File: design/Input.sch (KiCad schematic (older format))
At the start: 36 parts, among them J501 Conn_01x03, U501 93C46B, U502 FT4232H, U503 74LV595, X501 ASEMB-12MHz

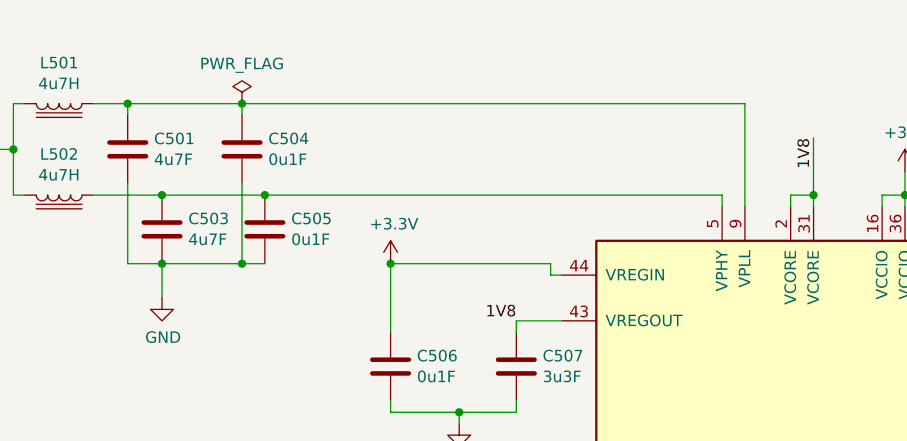
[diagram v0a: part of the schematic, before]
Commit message: Add 5V power to USB isolator
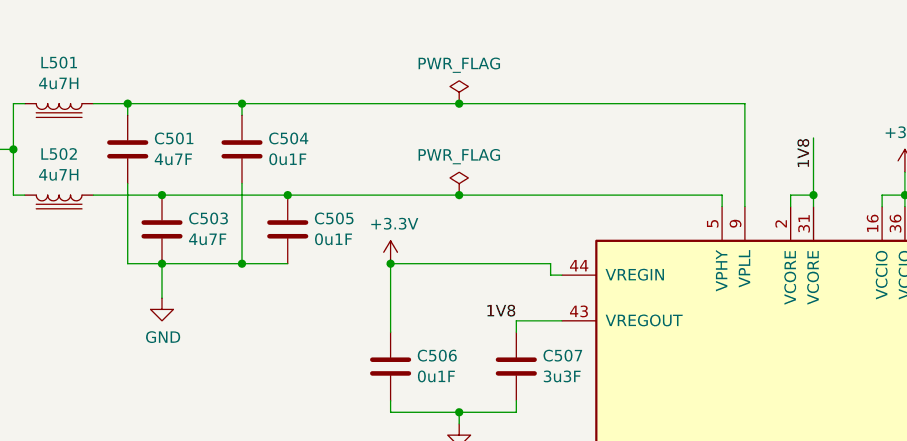
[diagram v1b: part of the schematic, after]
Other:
- moved on the sheet: C505
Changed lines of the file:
@@
 L Device:C C505
 U 1 1 5A772A13
-P 2500 1550
+P 2600 1550
 AR Path="/5A78E64E/5A772A13" Ref="C505"  Part="1"
 AR Path="/5A78E661/5A772A13" Ref="C705"  Part="1"
-F 0 "C505" H 2615 1596 50  0000 L CNN
-F 1 "0u1F" H 2615 1505 50  0000 L CNN
-F 2 "Capacitor_SMD:C_0603_1608Metric" H 2538 1400 50  0001 C CNN
-F 3 "http://www.samsungsem.com/kr/support/product-search/mlcc/CL10B104KO8WPNC.jsp" H 2500 1550 50  0001 C CNN
-F 4 "CL10B104KO8WPNC" H 2500 1550 50  0001 C CNN "mpn"
-	1    2500 1550
+F 0 "C505" H 2715 1596 50  0000 L CNN
+F 1 "0u1F" H 2715 1505 50  0000 L CNN
+F 2 "Capacitor_SMD:C_0603_1608Metric" H 2638 1400 50  0001 C CNN
+F 3 "http://www.samsungsem.com/kr/support/product-search/mlcc/CL10B104KO8WPNC.jsp" H 2600 1550 50  0001 C CNN
+F 4 "CL10B104KO8WPNC" H 2600 1550 50  0001 C CNN "mpn"
+	1    2600 1550
 	1    0    0    -1
 $EndComp
@@
 L power:PWR_FLAG #FLG0501
 U 1 1 5A8B20A8
-P 2400 1000
+P 3350 1000
 AR Path="/5A78E64E/5A8B20A8" Ref="#FLG0501"  Part="1"
 AR Path="/5A78E661/5A8B20A8" Ref="#FLG0701"  Part="1"
-F 0 "#FLG0701" H 2400 1075 50  0001 C CNN
-F 1 "PWR_FLAG" H 2400 1174 50  0000 C CNN
-F 2 "" H 2400 1000 50  0001 C CNN
-F 3 "" H 2400 1000 50  0001 C CNN
-	1    2400 1000
+F 0 "#FLG0701" H 3350 1075 50  0001 C CNN
+F 1 "PWR_FLAG" H 3350 1174 50  0000 C CNN
+F 2 "" H 3350 1000 50  0001 C CNN
+F 3 "" H 3350 1000 50  0001 C CNN
+	1    3350 1000
 	1    0    0    -1
 $EndComp
@@
 	1750 1400 2050 1400
 Wire Wire Line
-	2400 1000 4600 1000
-Wire Wire Line
-	2500 1400 4500 1400
-Wire Wire Line
-	2050 1400 2500 1400
+	2400 1000 3350 1000
+Wire Wire Line
+	2600 1400 3350 1400
 Connection ~ 2050 1400
 Connection ~ 1900 1000
@@
 Wire Wire Line
 	2050 1700 1900 1700
-Connection ~ 2500 1400
-Wire Wire Line
-	2400 1700 2500 1700
+Wire Wire Line
+	2400 1700 2600 1700
 Connection ~ 2400 1700
 Wire Wire Line
@@
 NoConn ~ 9550 3300
 NoConn ~ 9350 3300
+Connection ~ 2600 1400
+Wire Wire Line
+	2050 1400 2600 1400
+$Comp
+L power:PWR_FLAG #FLG0103
+U 1 1 5A985F6D
+P 3350 1400
+AR Path="/5A78E64E/5A985F6D" Ref="#FLG0103"  Part="1"
+AR Path="/5A78E661/5A985F6D" Ref="#FLG0104"  Part="1"
+F 0 "#FLG0104" H 3350 1475 50  0001 C CNN
+F 1 "PWR_FLAG" H 3350 1574 50  0000 C CNN
+F 2 "" H 3350 1400 50  0001 C CNN
+F 3 "" H 3350 1400 50  0001 C CNN
+	1    3350 1400
+	1    0    0    -1
+$EndComp
+Connection ~ 3350 1400
+Wire Wire Line
+	3350 1400 4500 1400
+Connection ~ 3350 1000
+Wire Wire Line
+	3350 1000 4600 1000
 $EndSCHEMATC

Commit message: Minimizing space in design
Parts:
- D501, D502, D503: footprint LED_THT:LED_D5.0mm-3 -> LEDs:WP130WDT
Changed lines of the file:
@@
 F 0 "D701" H 10550 3500 50  0000 C CNN
 F 1 "WP130WDT/EGW" H 10550 3584 50  0001 C CNN
-F 2 "LED_THT:LED_D5.0mm-3" H 10550 3250 50  0001 C CNN
+F 2 "LEDs:WP130WDT" H 10550 3250 50  0001 C CNN
 F 3 "http://www.kingbrightusa.com/images/catalog/SPEC/WP130WDT-EGW.pdf" H 10550 3250 50  0001 C CNN
 F 4 "WP130WDT/EGW" H 10550 3250 50  0001 C CNN "mpn"
@@
 F 0 "D702" H 10550 4000 50  0000 C CNN
 F 1 "WP130WDT/EGW" H 10550 4084 50  0001 C CNN
-F 2 "LED_THT:LED_D5.0mm-3" H 10550 3750 50  0001 C CNN
+F 2 "LEDs:WP130WDT" H 10550 3750 50  0001 C CNN
 F 3 "http://www.kingbrightusa.com/images/catalog/SPEC/WP130WDT-EGW.pdf" H 10550 3750 50  0001 C CNN
 F 4 "WP130WDT/EGW" H 10550 3750 50  0001 C CNN "mpn"
@@
 F 0 "D703" H 10550 4500 50  0000 C CNN
 F 1 "WP130WDT/EGW" H 10550 4584 50  0001 C CNN
-F 2 "LED_THT:LED_D5.0mm-3" H 10550 4250 50  0001 C CNN
+F 2 "LEDs:WP130WDT" H 10550 4250 50  0001 C CNN
 F 3 "http://www.kingbrightusa.com/images/catalog/SPEC/WP130WDT-EGW.pdf" H 10550 4250 50  0001 C CNN
 F 4 "WP130WDT/EGW" H 10550 4250 50  0001 C CNN "mpn"

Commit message: Switching to light pipes for LEDs
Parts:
- removed D502, D503: WP130WDT/EGW, LEDs:WP130WDT, symbol Device:LED_Dual_ACA
- added D502, D503: LTST-C155GYKT, LED_SMD:LED_RGB_1210, symbol Device:LED_Dual_AACC
- added LP501: LightPipe, LEDs:LightPipe DiaLight 515-1064, symbol CommsCard:LightPipe
- D501: value WP130WDT/EGW -> LTST-C155GYKT; footprint LEDs:WP130WDT -> LED_SMD:LED_RGB_1210; symbol Device:LED_Dual_ACA -> Device:LED_Dual_AACC; mpn WP130WDT/EGW -> LTST-C155GYKT
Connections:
- net GND: now also D503.3 (K1); no longer D501.2 (K)
- net at RN501.11 (R6.2): now also D501.2 (A2); no longer D501.1 (A1)
- net at RN501.12 (R5.2): now also D501.1 (A1); no longer D501.3 (A2)
- net at RN501.13 (R4.2): now also D502.2 (A2)
- net at RN501.14 (R3.2): now also D502.1 (A1)
- net at RN501.15 (R2.2): now also D503.2 (A2)
- net at RN501.16 (R1.2): now also D503.1 (A1)
- new net: D501.3 (K1), D501.4 (K2), D502.4 (K2)
- new net: D502.3 (K1), D503.4 (K2)
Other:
- moved on the sheet: D701
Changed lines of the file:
@@
 $Descr A4 11693 8268
 encoding utf-8
-Sheet 7 10
+Sheet 5 10
 Title ""
 Date ""
@@
 NoConn ~ 9950 3400
 $Comp
-L Device:LED_Dual_ACA D501
+L Device:LED_Dual_AACC D501
 U 1 1 5A834768
 P 10550 3250
@@
 AR Path="/5A78E661/5A834768" Ref="D701"  Part="1"
 F 0 "D701" H 10550 3500 50  0000 C CNN
-F 1 "WP130WDT/EGW" H 10550 3584 50  0001 C CNN
-F 2 "LEDs:WP130WDT" H 10550 3250 50  0001 C CNN
-F 3 "http://www.kingbrightusa.com/images/catalog/SPEC/WP130WDT-EGW.pdf" H 10550 3250 50  0001 C CNN
-F 4 "WP130WDT/EGW" H 10550 3250 50  0001 C CNN "mpn"
+F 1 "LTST-C155GYKT" H 10550 3584 50  0001 C CNN
+F 2 "LED_SMD:LED_RGB_1210" H 10550 3250 50  0001 C CNN
+F 3 "http://optoelectronics.liteon.com/upload/download/DS-22-98-0007/LTST-C155GYKT.pdf" H 10550 3250 50  0001 C CNN
+F 4 "LTST-C155GYKT" H 10550 3250 50  0001 C CNN "mpn"
 	1    10550 3250
-	-1   0    0    -1
+	1    0    0    1
 $EndComp
 $Comp
@@
 	1    0    0    -1
 $EndComp
-Wire Wire Line
-	10850 3250 10850 3750
-$Comp
-L Device:LED_Dual_ACA D502
-U 1 1 5A83C5E4
-P 10550 3750
-AR Path="/5A78E64E/5A83C5E4" Ref="D502"  Part="1"
-AR Path="/5A78E661/5A83C5E4" Ref="D702"  Part="1"
-F 0 "D702" H 10550 4000 50  0000 C CNN
-F 1 "WP130WDT/EGW" H 10550 4084 50  0001 C CNN
-F 2 "LEDs:WP130WDT" H 10550 3750 50  0001 C CNN
-F 3 "http://www.kingbrightusa.com/images/catalog/SPEC/WP130WDT-EGW.pdf" H 10550 3750 50  0001 C CNN
-F 4 "WP130WDT/EGW" H 10550 3750 50  0001 C CNN "mpn"
-	1    10550 3750
-	-1   0    0    -1
-$EndComp
-Connection ~ 10850 3750
-Wire Wire Line
-	10850 3750 10850 4250
-$Comp
-L Device:LED_Dual_ACA D503
-U 1 1 5A83C6A8
-P 10550 4250
-AR Path="/5A78E64E/5A83C6A8" Ref="D503"  Part="1"
-AR Path="/5A78E661/5A83C6A8" Ref="D703"  Part="1"
-F 0 "D703" H 10550 4500 50  0000 C CNN
-F 1 "WP130WDT/EGW" H 10550 4584 50  0001 C CNN
-F 2 "LEDs:WP130WDT" H 10550 4250 50  0001 C CNN
-F 3 "http://www.kingbrightusa.com/images/catalog/SPEC/WP130WDT-EGW.pdf" H 10550 4250 50  0001 C CNN
-F 4 "WP130WDT/EGW" H 10550 4250 50  0001 C CNN "mpn"
-	1    10550 4250
-	-1   0    0    -1
-$EndComp
-Connection ~ 10850 4250
-Wire Wire Line
-	10850 4250 10850 4500
 Wire Wire Line
 	9950 3500 10150 3500
@@
 Wire Wire Line
 	3350 1000 4600 1000
+Connection ~ 10850 3350
+Wire Wire Line
+	10850 3150 10850 3350
+Wire Wire Line
+	10850 3350 10850 3650
+$Comp
+L Device:LED_Dual_AACC D502
+U 1 1 5AB0129F
+P 10550 3750
+AR Path="/5A78E64E/5AB0129F" Ref="D502"  Part="1"
+AR Path="/5A78E661/5AB0129F" Ref="D702"  Part="1"
+F 0 "D702" H 10550 4000 50  0000 C CNN
+F 1 "LTST-C155GYKT" H 10550 4084 50  0001 C CNN
+F 2 "LED_SMD:LED_RGB_1210" H 10550 3750 50  0001 C CNN
+F 3 "http://optoelectronics.liteon.com/upload/download/DS-22-98-0007/LTST-C155GYKT.pdf" H 10550 3750 50  0001 C CNN
+F 4 "LTST-C155GYKT" H 10550 3750 50  0001 C CNN "mpn"
+	1    10550 3750
+	1    0    0    1
+$EndComp
+Wire Wire Line
+	10850 3850 10850 4150
+$Comp
+L Device:LED_Dual_AACC D503
+U 1 1 5AB0130B
+P 10550 4250
+AR Path="/5A78E64E/5AB0130B" Ref="D503"  Part="1"
+AR Path="/5A78E661/5AB0130B" Ref="D703"  Part="1"
+F 0 "D703" H 10550 4500 50  0000 C CNN
+F 1 "LTST-C155GYKT" H 10550 4584 50  0001 C CNN
+F 2 "LED_SMD:LED_RGB_1210" H 10550 4250 50  0001 C CNN
+F 3 "http://optoelectronics.liteon.com/upload/download/DS-22-98-0007/LTST-C155GYKT.pdf" H 10550 4250 50  0001 C CNN
+F 4 "LTST-C155GYKT" H 10550 4250 50  0001 C CNN "mpn"
+	1    10550 4250
+	1    0    0    1
+$EndComp
+Wire Wire Line
+	10850 4350 10850 4500
+$Comp
+L CommsCard:LightPipe LP501
+U 1 1 5AB0BDC0
+P 10450 2900
+AR Path="/5A78E64E/5AB0BDC0" Ref="LP501"  Part="1"
+AR Path="/5A78E661/5AB0BDC0" Ref="LP701"  Part="1"
+F 0 "LP701" V 10403 3080 50  0000 L CNN
+F 1 "LightPipe" V 10494 3080 50  0000 L CNN
+F 2 "LEDs:LightPipe DiaLight 515-1064" H 10462 2900 50  0001 C CNN
+F 3 "http://www.dialightsignalsandcomponents.com/Assets/Brochures_And_Catalogs/Indication/515-1064.pdf" H 10462 2900 50  0001 C CNN
+F 4 "5151064F" H 10450 2900 50  0001 C CNN "mpn"
+	1    10450 2900
+	0    1    1    0
+$EndComp
 $EndSCHEMATC
